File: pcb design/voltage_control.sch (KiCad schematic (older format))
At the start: 11 parts, among them Q19 PNP, U12 OPA2172

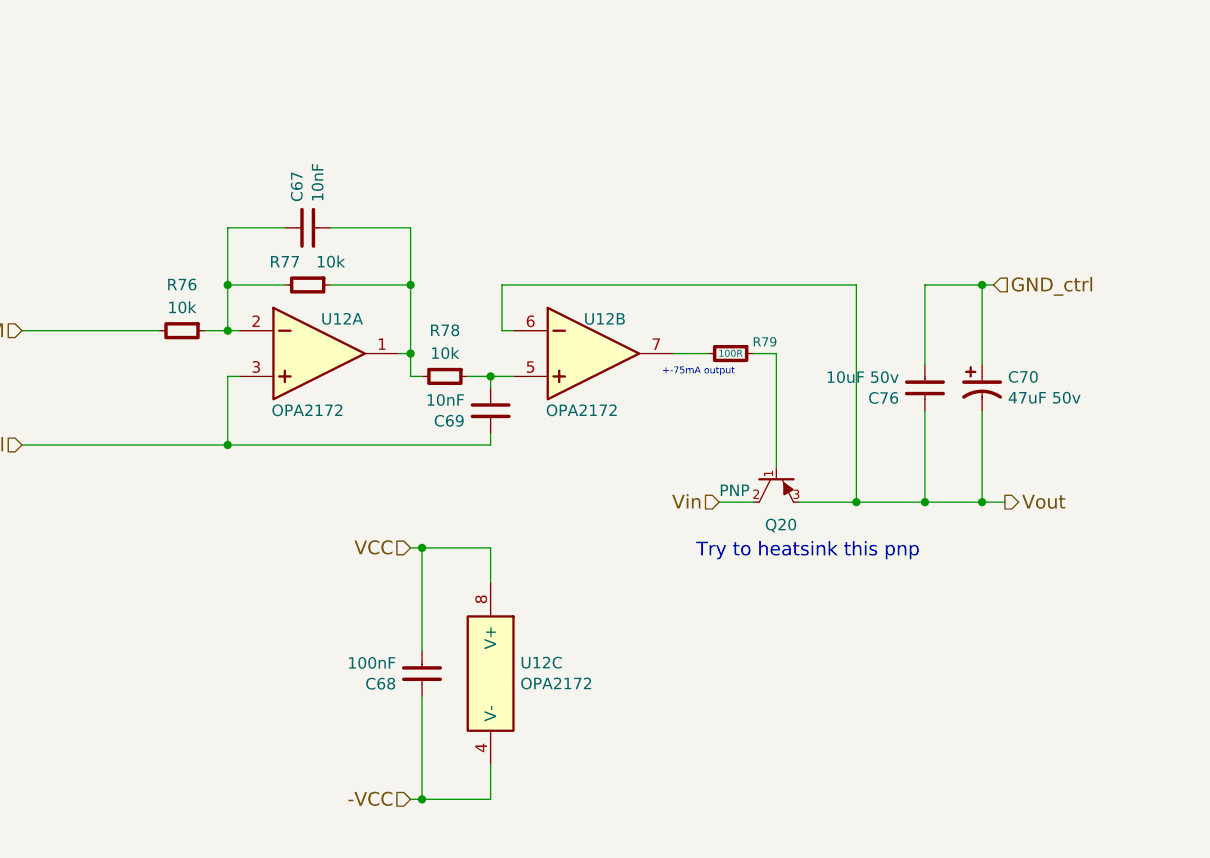
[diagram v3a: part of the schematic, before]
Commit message: Added comments before I forget things, changed X5R to X7R. Updated PCB
Signed-off-by: Marcos Chaparro <mchaparro@paltatech.com>
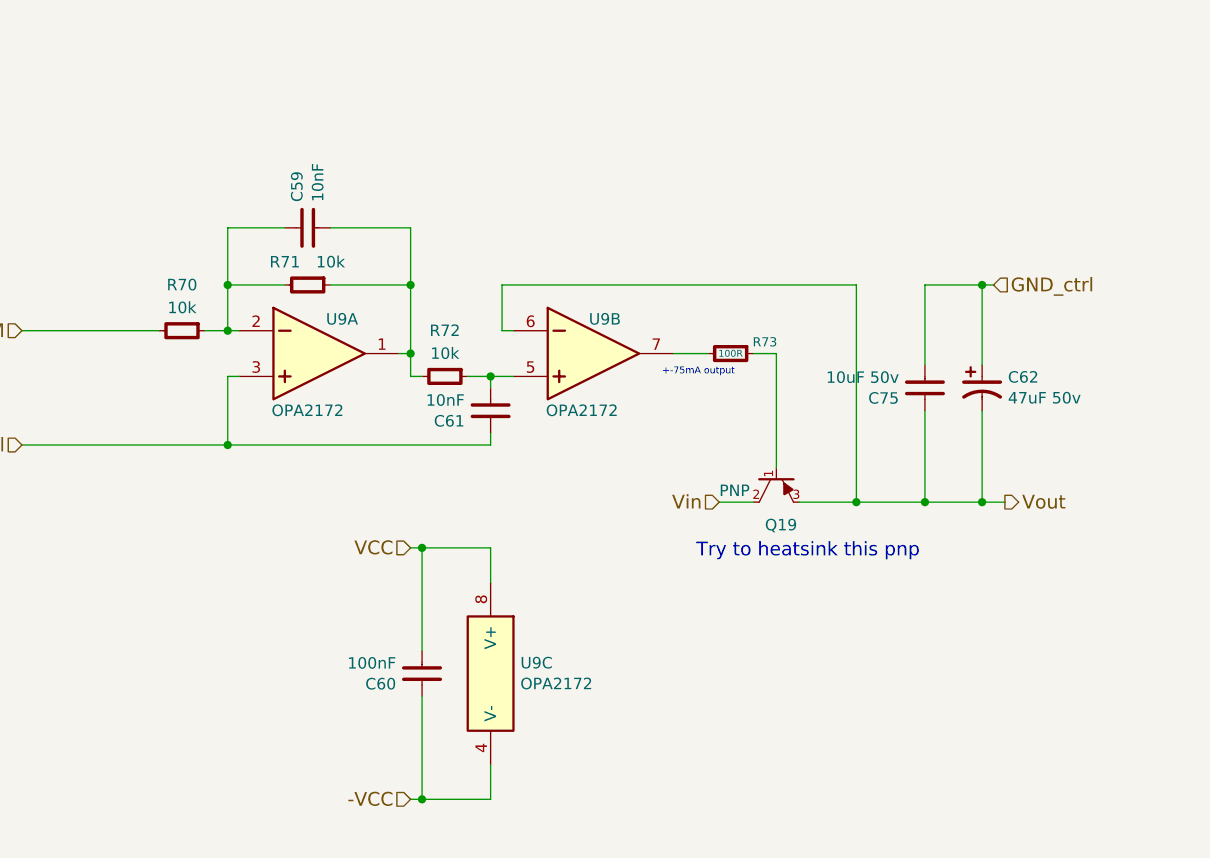
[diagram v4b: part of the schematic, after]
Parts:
- C75: mfg# CL31A106KBHNNNE -> CL31B106KBHNNNE
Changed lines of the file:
@@
 AR Path="/5822D62D/5856AA02/5856B1FC" Ref="Q19"  Part="1"
 AR Path="/5824556D/5856AA02/5856B1FC" Ref="Q20"  Part="1"
-F 0 "Q20" V 6900 3650 50  0000 L CNN
+F 0 "Q19" V 6900 3650 50  0000 L CNN
 F 1 "PNP" V 6750 3450 50  0000 L CNN
 F 2 "SMD_Packages:DPAK-2" H 6750 3700 60  0001 C CNN
@@
 AR Path="/5824556D/5856AA02/5856B214" Ref="R76"  Part="1"
 AR Path="/5822D62D/5856AA02/5856B214" Ref="R70"  Part="1"
-F 0 "R76" V 3950 3000 50  0000 C CNN
+F 0 "R70" V 3950 3000 50  0000 C CNN
 F 1 "10k" V 4050 3000 50  0000 C CNN
 F 2 "IPC7351-Nominal:RESC1608X50" H 4150 3000 50  0001 C CNN
@@
 AR Path="/5824556D/5856AA02/5856B21C" Ref="R77"  Part="1"
 AR Path="/5822D62D/5856AA02/5856B21C" Ref="R71"  Part="1"
-F 0 "R77" V 4600 2700 50  0000 C CNN
+F 0 "R71" V 4600 2700 50  0000 C CNN
 F 1 "10k" V 4600 2900 50  0000 C CNN
 F 2 "IPC7351-Nominal:RESC1608X50" H 4700 2800 50  0001 C CNN
@@
 AR Path="/5824556D/5856AA02/5856B237" Ref="C70"  Part="1"
 AR Path="/5822D62D/5856AA02/5856B237" Ref="C62"  Part="1"
-F 0 "C70" H 7763 3296 50  0000 L CNN
+F 0 "C62" H 7763 3296 50  0000 L CNN
 F 1 "47uF 50v" H 7763 3205 50  0000 L CNN
 F 2 "w_smd_cap:c_elec_6.3x7.7" H 7650 3250 50  0001 C CNN
@@
 AR Path="/5824556D/5856AA02/5856B245" Ref="C67"  Part="1"
 AR Path="/5822D62D/5856AA02/5856B245" Ref="C59"  Part="1"
-F 0 "C67" H 4813 2596 50  0000 L CNN
+F 0 "C59" H 4813 2596 50  0000 L CNN
 F 1 "10nF" H 4813 2505 50  0000 L CNN
 F 2 "IPC7351-Nominal:CAPC1608X55" H 4700 2550 50  0001 C CNN
@@
 AR Path="/5824556D/5856AA02/5856B251" Ref="R78"  Part="1"
 AR Path="/5822D62D/5856AA02/5856B251" Ref="R72"  Part="1"
-F 0 "R78" V 5100 3200 50  0000 C CNN
+F 0 "R72" V 5100 3200 50  0000 C CNN
 F 1 "10k" V 5200 3200 50  0000 C CNN
 F 2 "IPC7351-Nominal:RESC1608X50" H 5300 3200 50  0001 C CNN
@@
 AR Path="/5824556D/5856AA02/5856B25A" Ref="C69"  Part="1"
 AR Path="/5822D62D/5856AA02/5856B25A" Ref="C61"  Part="1"
-F 0 "C69" H 5613 3396 50  0000 L CNN
+F 0 "C61" H 5613 3396 50  0000 L CNN
 F 1 "10nF" H 5613 3305 50  0000 L CNN
 F 2 "IPC7351-Nominal:CAPC1608X55" H 5500 3350 50  0001 C CNN
@@
 AR Path="/5824556D/5856AA02/5856B26A" Ref="U12"  Part="1"
 AR Path="/5822D62D/5856AA02/5856B26A" Ref="U9"  Part="1"
-F 0 "U12" H 4850 3250 50  0000 C CNN
+F 0 "U9" H 4850 3250 50  0000 C CNN
 F 1 "OPA2172" H 4700 2850 50  0000 C CNN
 F 2 "IPC7351-Nominal:SOIC127P600X175-8" H 4700 2850 50  0001 C CNN
@@
 AR Path="/5824556D/5856AA02/5856B273" Ref="U12"  Part="2"
 AR Path="/5822D62D/5856AA02/5856B273" Ref="U9"  Part="2"
-F 0 "U12" H 6000 3250 50  0000 C CNN
+F 0 "U9" H 6000 3250 50  0000 C CNN
 F 1 "OPA2172" H 5900 2850 50  0000 C CNN
 F 2 "IPC7351-Nominal:SOIC127P600X175-8" H 5900 2850 50  0001 C CNN
@@
 AR Path="/5824556D/5856AA02/5856B5B6" Ref="U12"  Part="3"
 AR Path="/5822D62D/5856AA02/5856B5B6" Ref="U9"  Part="3"
-F 0 "U12" H 5630 4546 50  0000 L CNN
+F 0 "U9" H 5630 4546 50  0000 L CNN
 F 1 "OPA2172" H 5630 4455 50  0000 L CNN
 F 2 "IPC7351-Nominal:SOIC127P600X175-8" H 5500 4250 50  0001 C CNN
@@
 AR Path="/5824556D/5856AA02/5856B5EA" Ref="C68"  Part="1"
 AR Path="/5822D62D/5856AA02/5856B5EA" Ref="C60"  Part="1"
-F 0 "C68" H 5313 4546 50  0000 L CNN
+F 0 "C60" H 5313 4546 50  0000 L CNN
 F 1 "100nF" H 5313 4455 50  0000 L CNN
 F 2 "IPC7351-Nominal:CAPC1608X55" H 5200 4500 50  0001 C CNN
@@
 AR Path="/5822D62D/5856AA02/58575342" Ref="R73"  Part="1"
 AR Path="/5824556D/5856AA02/58575342" Ref="R79"  Part="1"
-F 0 "R79" V 6500 3250 40  0000 C CNN
+F 0 "R73" V 6500 3250 40  0000 C CNN
 F 1 "100R" V 6550 3100 30  0000 C CNN
 F 2 "IPC7351-Nominal:RESC2012X50" H 6550 3100 50  0001 C CNN
@@
 AR Path="/5822D62D/5856AA02/5858F095" Ref="C75"  Part="1"
 AR Path="/5824556D/5856AA02/5858F095" Ref="C76"  Part="1"
-F 0 "C76" H 7513 3296 50  0000 L CNN
+F 0 "C75" H 7513 3296 50  0000 L CNN
 F 1 "10uF 50v" H 7513 3205 50  0000 L CNN
 F 2 "IPC7351-Nominal:CAPC3216X70" H 7400 3250 50  0001 C CNN
 F 3 "" H 7390 3225 60  0000 C CNN
-F 4 "CL31A106KBHNNNE" H 7400 3250 60  0001 C CNN "mfg#"
+F 4 "CL31B106KBHNNNE" H 7400 3250 60  0001 C CNN "mfg#"
 	1    7400 3250
 	-1   0    0    1

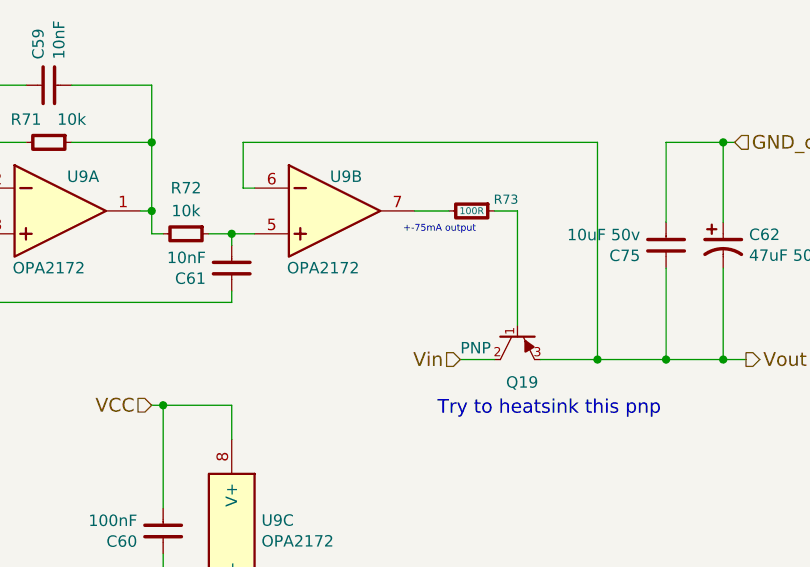
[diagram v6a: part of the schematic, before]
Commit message: Added current sensor connector. Layout is now symmetrical
Signed-off-by: Marcos Chaparro <mchaparro@paltatech.com>
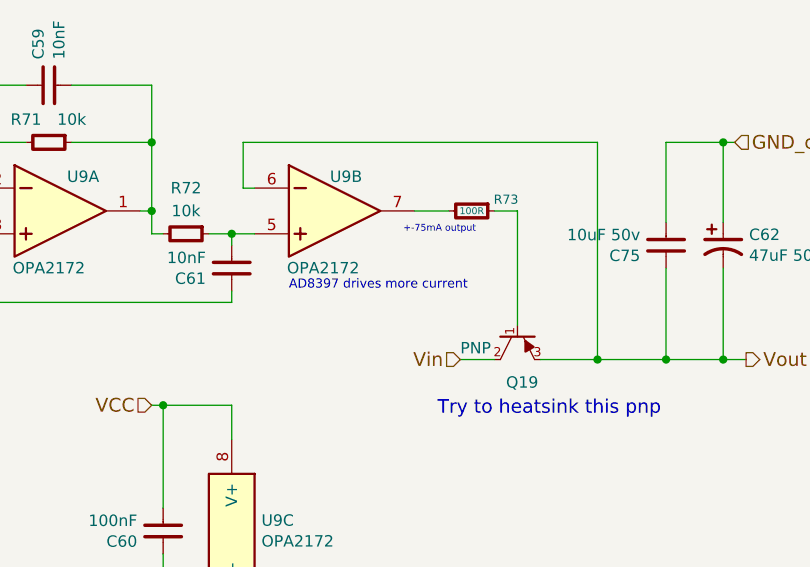
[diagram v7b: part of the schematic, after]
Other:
- note added: "AD8397 drives more current"
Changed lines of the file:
@@
 $Bitmap
 Pos 5600 6700
-Scale 1.000000
+Scale 1,000000
 Data
 89 50 4E 47 0D 0A 1A 0A 00 00 00 0D 49 48 44 52 00 00 03 13 00 00 02 55 08 02 00 00 00 2A 4E 3F
@@
 $Bitmap
 Pos 2250 6750
-Scale 1.000000
+Scale 1,000000
 Data
 89 50 4E 47 0D 0A 1A 0A 00 00 00 0D 49 48 44 52 00 00 03 C3 00 00 02 4A 08 02 00 00 00 87 DF 00
@@
 Text Notes 6400 4000 0    60   ~ 0
 Try to heatsink this pnp
+Text Notes 5750 3450 0    40   ~ 0
+AD8397 drives more current
 $EndSCHEMATC

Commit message: Add gate driver load to enable 2 step turnoff in buffered configuration. Updated layout.
Signed-off-by: Marcos Chaparro <mchaparro@paltatech.com>
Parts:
- C67, C68, C69: symbol C-0603 -> pasv-cap:C-0603
- C70: symbol C-ALUM-6.3mm -> pasv-cap:C-ALUM-6.3mm; MPN (none) -> EEE-FK1H470XP
- C75: symbol C-1206 -> pasv-cap:C-1206; MPN (none) -> CL31A106KBHNNNE; mfg# CL31B106KBHNNNE -> CL31A106KBHNNNE
- Q19: symbol PNP -> _semi:PNP; MPN (none) -> MJD2955T4G
- R73: symbol R-0805 -> pasv-res:R-0805
- R76, R77, R78: symbol R-0603 -> pasv-res:R-0603
- U12: symbol OPA2376AID -> TexasInstruments:OPA2376AID; MPN (none) -> OPA2172IDR
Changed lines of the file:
@@
-EESchema Schematic File Version 2
-LIBS:Abracon
-LIBS:ActiveSemi
-LIBS:Altera
-LIBS:AMS
-LIBS:AnalogDevices
-LIBS:AOS
-LIBS:Atmel
-LIBS:Bosch
-LIBS:conn-100mil
-LIBS:conn-2mm
-LIBS:conn-amphenol
-LIBS:conn-assmann
-LIBS:conn-cui
-LIBS:conn-fci
-LIBS:conn-jae
-LIBS:conn-linx
-LIBS:conn-molex
-LIBS:conn-tagconnect
-LIBS:conn-te
-LIBS:conn-test
-LIBS:DiodesInc
-LIBS:display
-LIBS:electomech-misc
-LIBS:_electromech
-LIBS:Fairchild
-LIBS:FTDI
-LIBS:Infineon
-LIBS:Intersil
-LIBS:Lattice
-LIBS:_linear
-LIBS:LinearTech
-LIBS:Littelfuse
-LIBS:logic-4000
-LIBS:logic-7400
-LIBS:logic-7400-new
-LIBS:_logic
-LIBS:MACOM
-LIBS:Macrofab
-LIBS:maxim
-LIBS:mechanical
-LIBS:Microchip
-LIBS:Micron
-LIBS:Murata
-LIBS:NXP
-LIBS:OceanOptics
-LIBS:onsemi
-LIBS:_passive
-LIBS:pasv-BelFuse
-LIBS:pasv-BiTech
-LIBS:pasv-Bourns
-LIBS:pasv-cap
-LIBS:pasv-ind
-LIBS:pasv-Murata
-LIBS:pasv-res
-LIBS:pasv-TDK
-LIBS:pasv-xtal
-LIBS:pcb
-LIBS:power
-LIBS:Recom
-LIBS:Richtek
-LIBS:semi-diode-DiodesInc
-LIBS:semi-diode-generic
-LIBS:semi-diode-MCC
-LIBS:semi-diode-NXP
-LIBS:semi-diode-OnSemi
-LIBS:semi-diode-Semtech
-LIBS:semi-diode-ST
-LIBS:semi-diode-Toshiba
-LIBS:_semi
-LIBS:semi-opto-generic
-LIBS:semi-opto-liteon
-LIBS:semi-thyristor-generic
-LIBS:semi-trans-AOS
-LIBS:semi-trans-DiodesInc
-LIBS:semi-trans-EPC
-LIBS:semi-trans-Fairchild
-LIBS:semi-trans-generic
-LIBS:semi-trans-Infineon
-LIBS:semi-trans-IRF
-LIBS:semi-trans-IXYS
-LIBS:semi-trans-NXP
-LIBS:semi-trans-OnSemi
-LIBS:semi-trans-Panasonic
-LIBS:semi-trans-ST
-LIBS:semi-trans-TI
-LIBS:semi-trans-Toshiba
-LIBS:semi-trans-Vishay
-LIBS:silabs
-LIBS:skyworks
-LIBS:st_ic
-LIBS:ST
-LIBS:supertex
-LIBS:symbol
-LIBS:TexasInstruments
-LIBS:u-blox
-LIBS:Vishay
-LIBS:Winbond
-LIBS:Xilinx
-LIBS:paltatech
+EESchema Schematic File Version 4
 LIBS:IGBT_board-cache
 EELAYER 26 0
@@
 $EndDescr
 $Comp
-L PNP Q19
+L _semi:PNP Q19
 U 1 1 5856B1FC
 P 6750 3700
@@
 F 3 "" H 6750 3700 60  0000 C CNN
 F 4 "MJD2955T4G" H 6750 3700 60  0001 C CNN "mfg#"
+F 5 "MJD2955T4G" H 0   0   60  0001 C CNN "MPN"
 	1    6750 3700
 	0    1    1    0
@@
 	4350 3200 4400 3200
 $Comp
-L R-0603 R?
+L pasv-res:R-0603 R?
 U 1 1 5856B214
 P 4150 3000
@@
 $EndComp
 $Comp
-L R-0603 R?
+L pasv-res:R-0603 R?
 U 1 1 5856B21C
 P 4700 2800
@@
 Connection ~ 7100 3750
 $Comp
-L C-ALUM-6.3mm C?
+L pasv-cap:C-ALUM-6.3mm C?
 U 1 1 5856B237
 P 7650 3250
@@
 F 3 "" H 7640 3225 60  0000 C CNN
 F 4 "EEE-FK1H470XP" H 7650 3250 60  0001 C CNN "mfg#"
+F 5 "EEE-FK1H470XP" H 0   0   60  0001 C CNN "MPN"
 	1    7650 3250
 	1    0    0    -1
@@
 	3450 3000 4050 3000
 $Comp
-L C-0603 C?
+L pasv-cap:C-0603 C?
 U 1 1 5856B245
 P 4700 2550
@@
 Connection ~ 4350 2800
 $Comp
-L R-0603 R?
+L pasv-res:R-0603 R?
 U 1 1 5856B251
 P 5300 3200
@@
 	5150 3200 5200 3200
 $Comp
-L C-0603 C?
+L pasv-cap:C-0603 C?
 U 1 1 5856B25A
 P 5500 3350
@@
 Connection ~ 4350 3500
 $Comp
-L OPA2376AID U?
+L TexasInstruments:OPA2376AID U?
 U 1 1 5856B26A
 P 4700 3100
@@
 F 4 "OPA2172IDR" H 4700 3100 60  0001 C CNN "#mfg"
 F 5 "IC TI OPA2376AID" H 4700 2750 60  0001 C CNN "BOM"
+F 6 "OPA2172IDR" H 0   0   60  0001 C CNN "MPN"
 	1    4700 3100
 	1    0    0    -1
 $EndComp
 $Comp
-L OPA2376AID U?
+L TexasInstruments:OPA2376AID U?
 U 2 1 5856B273
 P 5900 3100
@@
 F 4 "OPA2172IDR" H 5900 3100 60  0001 C CNN "#mfg"
 F 5 "IC TI OPA2376AID" H 5900 2750 60  0001 C CNN "BOM"
+F 6 "OPA2172IDR" H 0   0   60  0001 C CNN "MPN"
 	2    5900 3100
 	1    0    0    -1
 $EndComp
 $Comp
-L OPA2376AID U?
+L TexasInstruments:OPA2376AID U?
 U 3 1 5856B5B6
 P 5500 4500
@@
 F 4 "OPA2172IDR" H 5500 4500 60  0001 C CNN "#mfg"
 F 5 "IC TI OPA2376AID" H 5500 4150 60  0001 C CNN "BOM"
+F 6 "OPA2172IDR" H 0   0   60  0001 C CNN "MPN"
 	3    5500 4500
 	1    0    0    -1
 $EndComp
 $Comp
-L C-0603 C?
+L pasv-cap:C-0603 C?
 U 1 1 5856B5EA
 P 5200 4500
@@
 +-75mA output
 $Comp
-L R-0805 R73
+L pasv-res:R-0805 R73
 U 1 1 58575342
 P 6550 3100
@@
 $EndComp
 $Comp
-L C-1206 C?
+L pasv-cap:C-1206 C?
 U 1 1 5858F095
 P 7400 3250
@@
 F 2 "IPC7351-Nominal:CAPC3216X70" H 7400 3250 50  0001 C CNN
 F 3 "" H 7390 3225 60  0000 C CNN
-F 4 "CL31B106KBHNNNE" H 7400 3250 60  0001 C CNN "mfg#"
+F 4 "CL31A106KBHNNNE" H 7400 3250 60  0001 C CNN "mfg#"
+F 5 "CL31A106KBHNNNE" H 0   0   60  0001 C CNN "MPN"
 	1    7400 3250
 	-1   0    0    1
